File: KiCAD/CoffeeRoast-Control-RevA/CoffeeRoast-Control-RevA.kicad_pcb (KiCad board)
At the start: 2 copper layers, 100 x 75 mm, 26 parts, among them J1 24V_IN_FROM_230V_PSU_3A, J2 FAN_24V_PWM_3A, J3 SSR_INPUT_TO_EXTERNAL_SSR, J4 K_TYPE_THERMOCOUPLE, J5 USB_DATA_PANEL_HEADER, Q1 IRLZ44N_OR_LOGIC_NMOS, Q2 2N7002_SSR_DRIVER, SW1 RESET_EN, SW2 BOOT, U1 ESP32-S3-WROOM-1, U2 MAX6675_SOIC8_3V3, U3 AMS1117-3.3, U4 24V_TO_5V_BUCK_MODULE_>=1A

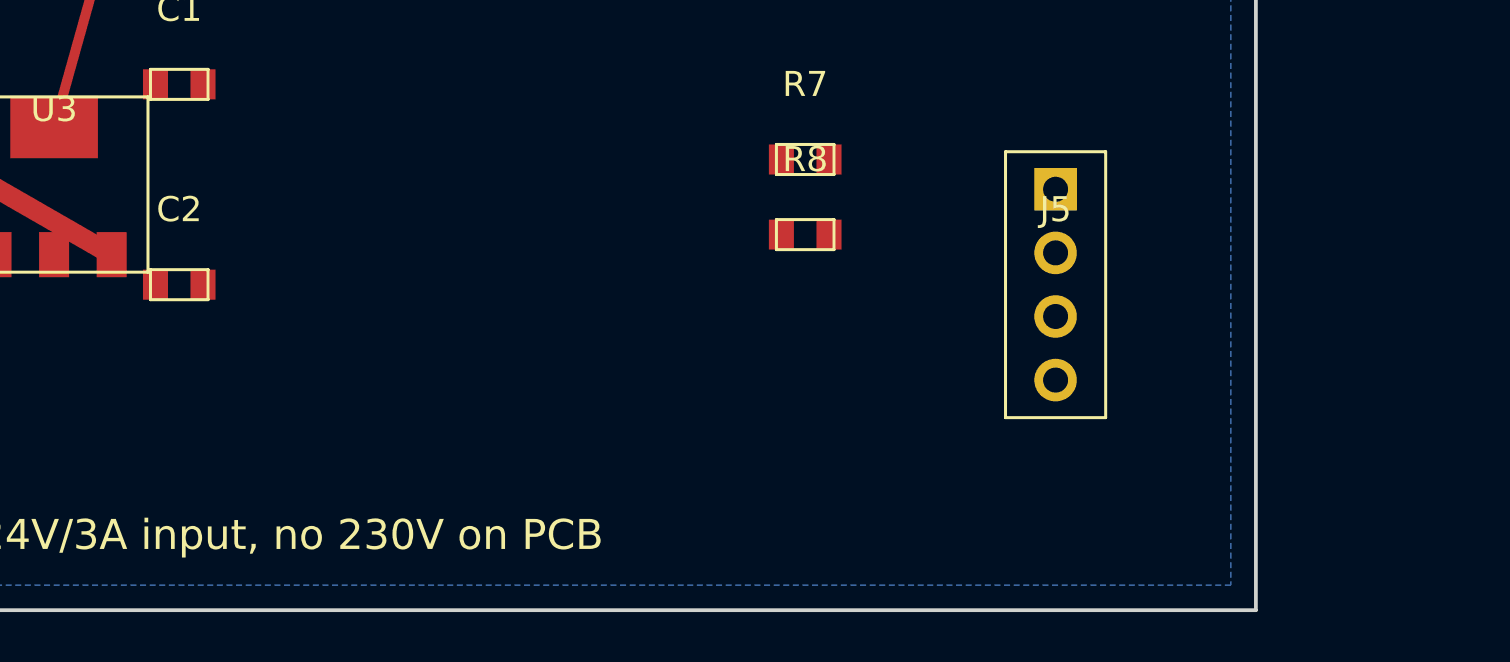
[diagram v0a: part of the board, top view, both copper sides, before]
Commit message: Put USB-C connector on CoffeeRoast control PCB
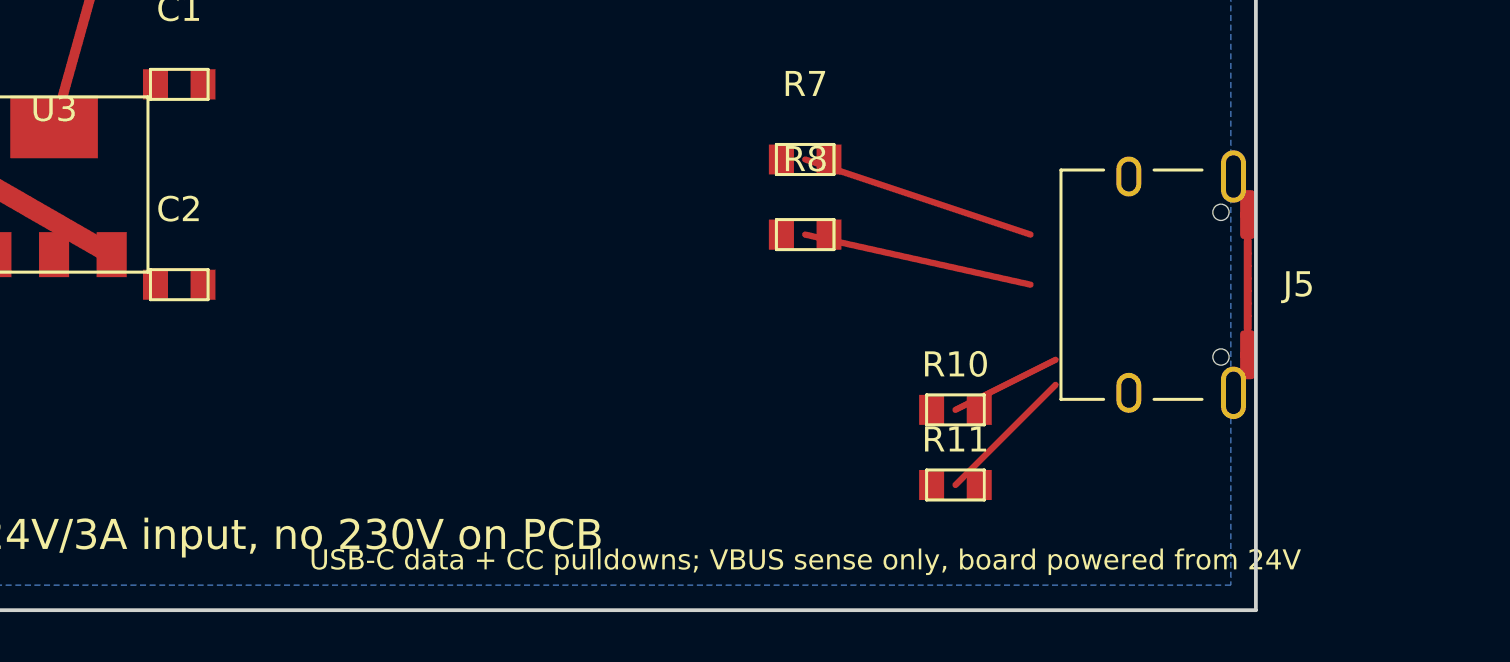
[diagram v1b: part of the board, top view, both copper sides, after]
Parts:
- added R10: 5k1_CC1_RD, CoffeeRoast:R_0805, F.Cu at (88.0, 67.0)
- added R11: 5k1_CC2_RD, CoffeeRoast:R_0805, F.Cu at (88.0, 70.0)
- J5: value USB_DATA_PANEL_HEADER -> USB_C_Receptacle_XKB_U262-16XN-4BVC11; footprint CoffeeRoast:PinHeader_1x4_P2.54mm -> Connector_USB:USB_C_Receptacle_XKB_U262-16XN-4BVC11
- moved J5 4.00 mm to (96.0, 62.0), turned to -90 degrees
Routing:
- net USB_DN: track 0.00 -> 9.49 mm
- net USB_DP: track 0.00 -> 9.22 mm
- net USB_CC2: track 0.00 -> 5.66 mm
- net USB_CC1: track 0.00 -> 4.47 mm
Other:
- board text added: "USB-C data + CC pulldowns; VBUS sense only, board powered from 24V"

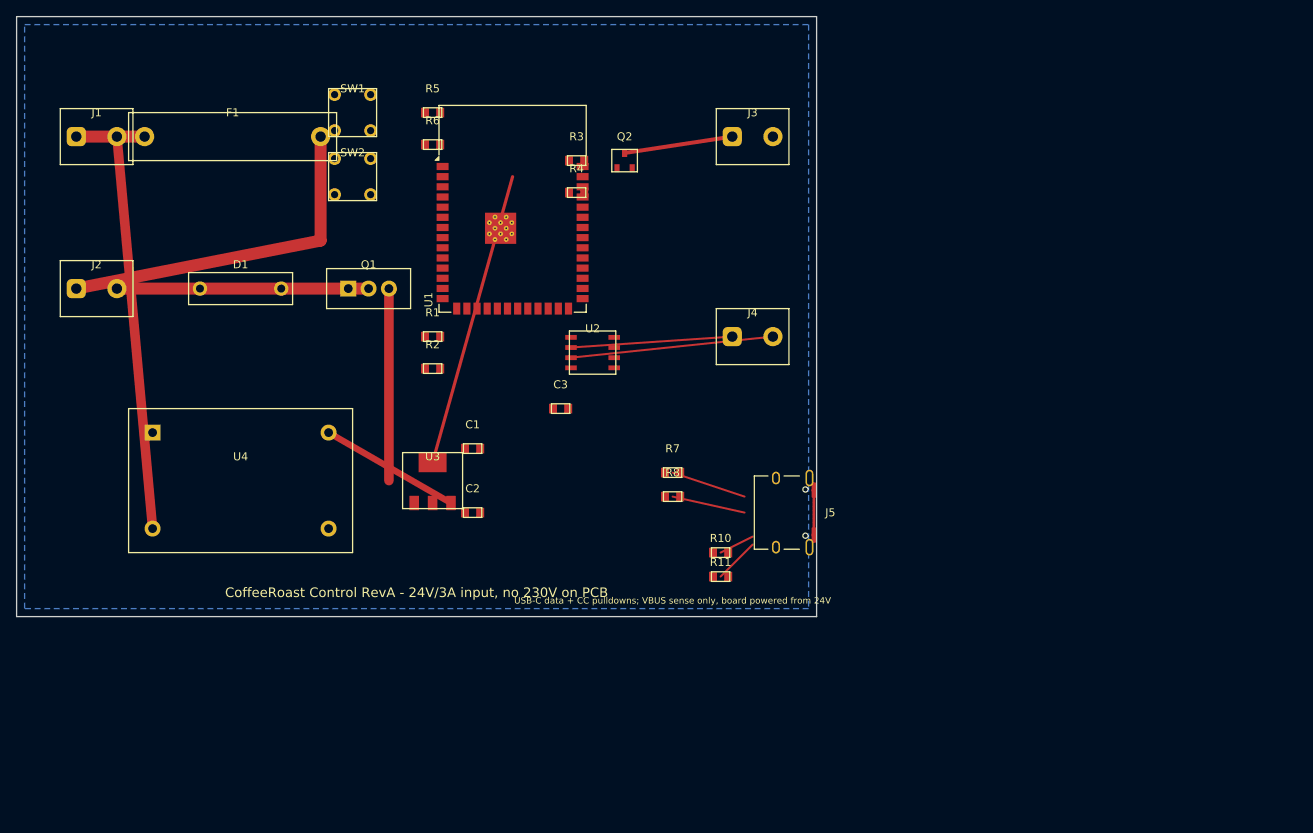
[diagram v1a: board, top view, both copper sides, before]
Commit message: Render CoffeeRoast PCB with KiCad
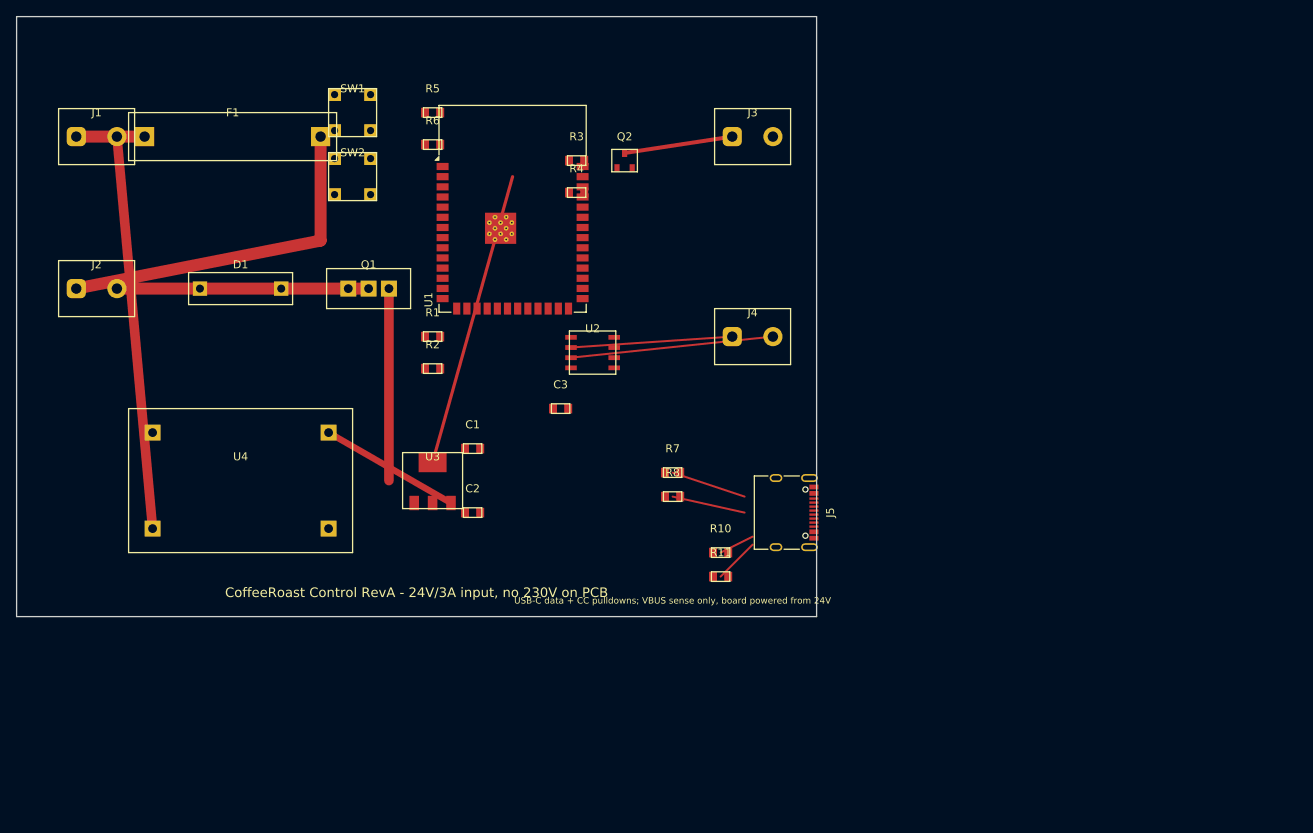
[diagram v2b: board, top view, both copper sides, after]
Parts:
- C1, C2, C3: footprint CoffeeRoast:C_0805 -> (none)
- D1: footprint CoffeeRoast:Diode_THT_P10.16mm -> (none)
- F1: footprint CoffeeRoast:Fuseholder_5x20mm_inline -> (none)
- J1, J2, J3, J4: footprint CoffeeRoast:TerminalBlock_2P_5.08mm -> (none)
- J5: footprint Connector_USB:USB_C_Receptacle_XKB_U262-16XN-4BVC11 -> USB_C_Receptacle_XKB_U262-16XN-4BVC11
- Q1: footprint CoffeeRoast:TO-220-3_Vertical -> (none)
- Q2: footprint CoffeeRoast:SOT-23 -> (none)
- R1, R10, R11, R2, R3, R4, R5, R6, R7, R8: footprint CoffeeRoast:R_0805 -> (none)
- SW1, SW2: footprint CoffeeRoast:SW_Tactile_6x6mm -> (none)
- U1: footprint RF_Module:ESP32-S3-WROOM-1 -> ESP32-S3-WROOM-1
- U2: footprint CoffeeRoast:SOIC-8_3.9x4.9mm_P1.27mm -> (none)
- U3: footprint CoffeeRoast:SOT-223-3_TabPin2 -> (none)
- U4: footprint CoffeeRoast:Buck_Module_24V_to_5V_4Pin -> (none)
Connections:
- U2 pad 8: (no net) -> GND
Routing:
- net GND: track 73.2 -> 83.3 mm
- net USB_CC2: track 5.66 -> 0.00 mm
- net USB_CC1: track 4.47 -> 0.00 mm
- removed copper zone on B.Cu, net GND

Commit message: Autoroute CoffeeRoast control PCB
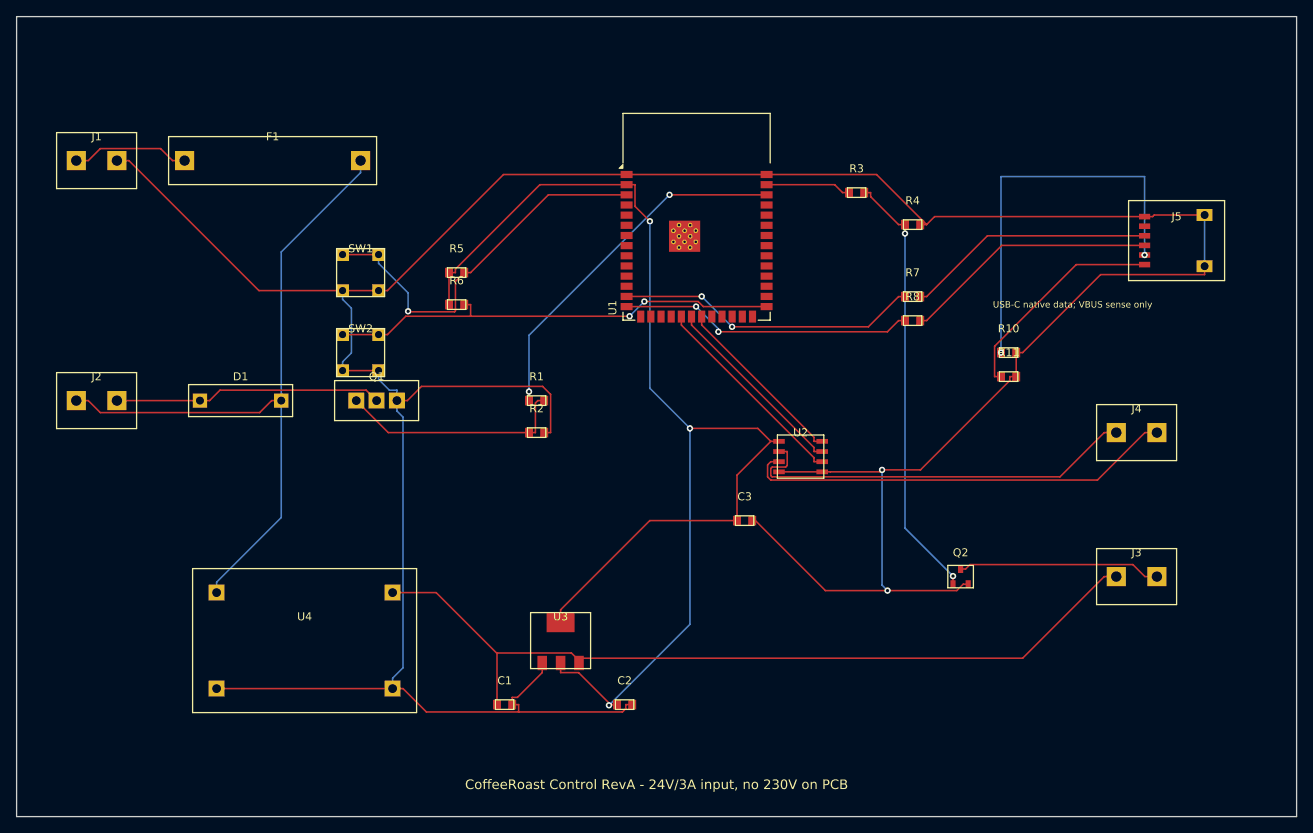
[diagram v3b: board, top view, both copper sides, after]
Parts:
- J5: value USB_C_Receptacle_XKB_U262-16XN-4BVC11 -> USB_C_RECEPTACLE_DRAFT_6PIN; footprint USB_C_Receptacle_XKB_U262-16XN-4BVC11 -> (none)
- moved J3 73.0 mm to (140.0, 70.0)
- moved Q2 66.8 mm to (118.0, 70.0)
- moved J5 59.6 mm to (145.0, 28.0), turned to 0 degrees
- moved J4 49.5 mm to (140.0, 52.0)
- moved R10 43.8 mm to (124.0, 42.0)
- moved R11 43.8 mm to (124.0, 45.0)
- moved R4 42.2 mm to (112.0, 26.0)
- moved R7 37.2 mm to (112.0, 35.0)
- moved R8 37.2 mm to (112.0, 38.0)
- moved R3 35.2 mm to (105.0, 22.0)
- moved C1 32.2 mm to (61.0, 86.0)
- moved C2 30.6 mm to (76.0, 86.0)
- moved U2 29.1 mm to (98.0, 55.0)
- moved C3 26.9 mm to (91.0, 63.0)
- moved U3 25.6 mm to (68.0, 78.0)
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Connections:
- J5 pad S1: (no net) -> GND
- U1 pad 41: GND -> (no net)
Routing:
- net GND: track 83.3 -> 418.0 mm, vias 0 -> 2
- net +3V3: track 37.1 -> 166.0 mm, vias 0 -> 3
- net +5V: track 17.7 -> 105.2 mm
- net BOOT: track 0.00 -> 57.2 mm, vias 0 -> 2
- net SSR_GATE: track 0.00 -> 54.5 mm, vias 0 -> 2
- net USB_CC1: track 0.00 -> 49.8 mm, vias 0 -> 2
- net EN: track 0.00 -> 48.7 mm, vias 0 -> 1
- net FAN_PWM: track 0.00 -> 45.1 mm, vias 0 -> 2
- net +24V_FUSED: track 44.1 -> 88.3 mm
- net USB_DN_MCU: track 0.00 -> 37.9 mm, vias 0 -> 2
- net USB_DP_MCU: track 0.00 -> 36.9 mm, vias 0 -> 2
- net THERMO_PLUS: track 20.2 -> 51.4 mm
- net THERMO_MINUS: track 25.4 -> 54.4 mm
- net FAN_GATE: track 0.00 -> 29.0 mm
- net USB_CC2: track 0.00 -> 27.6 mm
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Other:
- board size 100 x 75 mm -> 160 x 100 mm
- board text added: "ESP32 ANTENNA KEEPOUT - no copper"
- board text added: "USB-C native data; VBUS sense only"
- board text removed: "ESP32 ANTENNA KEEPOUT - no copper / keep at board edge"
- board text removed: "USB-C data + CC pulldowns; VBUS sense only, board powered from 24V"

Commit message: Replace USB-C draft with exact connector footprint
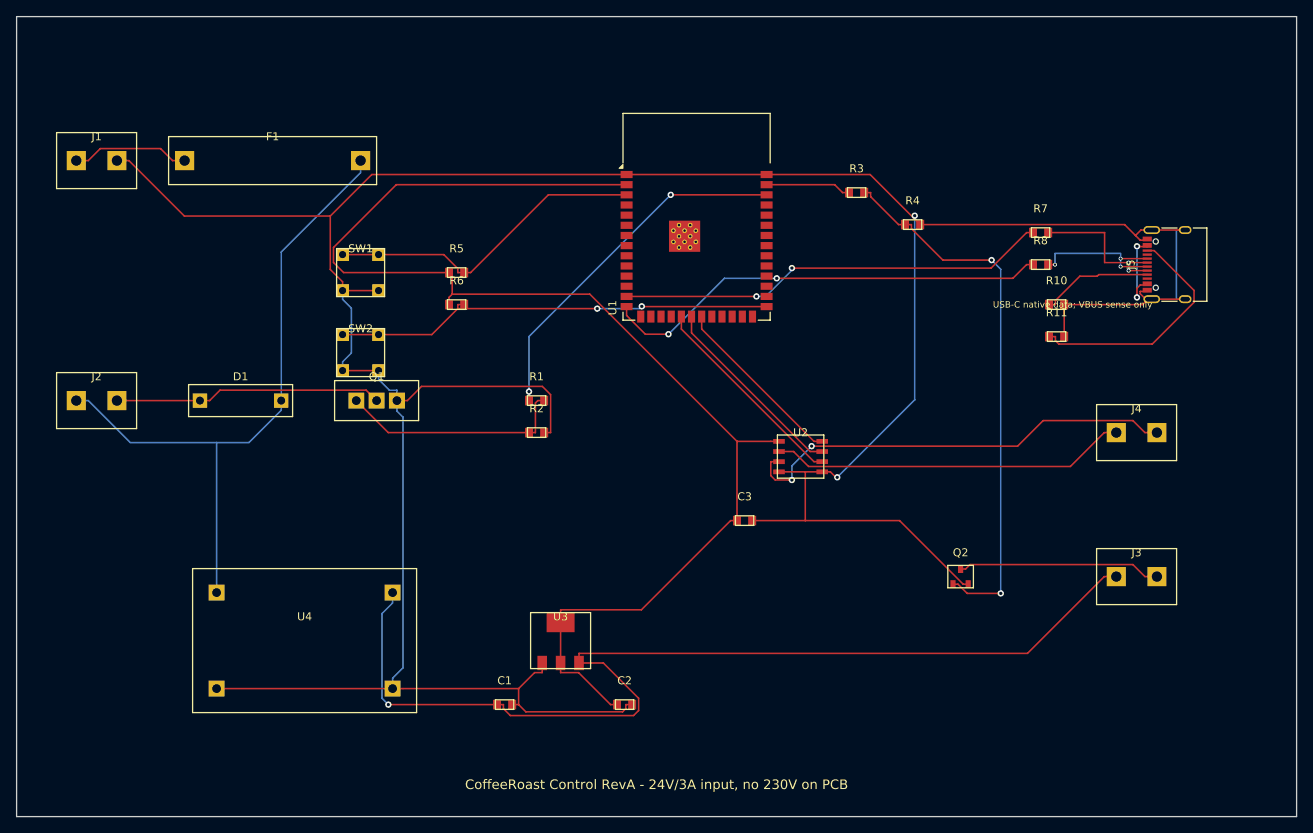
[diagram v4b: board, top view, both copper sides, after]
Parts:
- J5: value USB_C_RECEPTACLE_DRAFT_6PIN -> USB_C_Receptacle_XKB_U262-16XN-4BVC11; footprint (none) -> USB_C_Receptacle_XKB_U262-16XN-4BVC11
- moved R7 17.9 mm to (128.0, 27.0)
- moved R8 17.5 mm to (128.0, 31.0)
- moved R10 8.49 mm to (130.0, 36.0)
- moved R11 7.81 mm to (130.0, 40.0)
- moved J5 3.00 mm to (145.0, 31.0), turned to 90 degrees
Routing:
- net USB_CC1: track 49.8 -> 14.1 mm, vias 2 -> 0
- net +5V: track 105.2 -> 130.4 mm, vias 0 -> 1
- net USB_DP_MCU: track 36.9 -> 56.5 mm
- net USB_DN_MCU: track 37.9 -> 54.3 mm
- net SSR_GATE: track 54.5 -> 68.6 mm
- net USB_DP: track 31.9 -> 18.8 mm, vias 0 -> 3
- net USB_DN: track 31.2 -> 19.5 mm, vias 0 -> 2
- net USB_VBUS: track 0.00 -> 10.9 mm, vias 0 -> 2
- net EN: track 48.7 -> 40.8 mm, vias 1 -> 0
- net THERMO_PLUS: track 51.4 -> 44.7 mm
- net +24V_FUSED: track 88.3 -> 83.5 mm
- net +3V3: track 166.0 -> 162.9 mm, vias 3 -> 0
- net USB_CC2: track 27.6 -> 30.4 mm
- net THERMO_MINUS: track 54.4 -> 56.0 mm, vias 0 -> 2
- net BOOT: track 57.2 -> 55.8 mm
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
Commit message: Expose ESP32 pins as debug pads
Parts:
- added TPESP1: GND, , F.Cu at (75.3, 19.7)
- added TPESP10: IO17, , F.Cu at (75.3, 31.2)
- added TPESP11: IO18, , F.Cu at (75.3, 32.4)
- added TPESP12: IO8, , F.Cu at (75.3, 33.7)
- added TPESP13: USB_D-/IO19, , F.Cu at (75.3, 35.0)
- added TPESP14: USB_D+/IO20, , F.Cu at (75.3, 36.2)
- added TPESP15: IO3, , F.Cu at (78.0, 38.3)
- added TPESP16: IO46, , F.Cu at (79.3, 38.5)
- added TPESP17: IO9, , F.Cu at (80.6, 38.5)
- added TPESP18: IO10, , F.Cu at (81.8, 38.5)
- added TPESP19: IO11/MAXDO, , F.Cu at (83.1, 38.5)
- added TPESP2: 3V3, , F.Cu at (75.3, 21.0)
- added TPESP20: IO12/MAXCS, , F.Cu at (84.4, 38.5)
- added TPESP21: IO13/MAXCLK, , F.Cu at (85.6, 38.5)
- added TPESP22: IO14, , F.Cu at (86.9, 38.5)
- added TPESP23: IO21, , F.Cu at (88.2, 38.5)
- added TPESP24: IO47, , F.Cu at (89.4, 38.5)
- added TPESP25: IO48, , F.Cu at (90.7, 38.5)
- added TPESP26: IO45, , F.Cu at (92.0, 38.5)
- added TPESP27: IO0/BOOT, , F.Cu at (94.7, 36.2)
- added TPESP28: IO35, , F.Cu at (94.7, 35.0)
- added TPESP29: IO36, , F.Cu at (94.7, 33.7)
- added TPESP3: EN, , F.Cu at (75.3, 22.3)
- added TPESP30: IO37, , F.Cu at (94.2, 32.4)
- added TPESP31: IO38, , F.Cu at (94.7, 31.2)
- added TPESP32: IO39, , F.Cu at (94.7, 29.9)
- added TPESP33: IO40, , F.Cu at (94.7, 28.6)
- added TPESP34: IO41, , F.Cu at (94.7, 27.4)
- added TPESP35: IO42, , F.Cu at (94.7, 26.1)
- added TPESP36: RXD0/IO44, , F.Cu at (94.7, 24.8)
- added TPESP37: TXD0/IO43, , F.Cu at (94.7, 23.6)
- added TPESP38: IO2/FAN, , F.Cu at (94.7, 22.3)
- added TPESP39: IO1/SSR, , F.Cu at (94.7, 21.0)
- added TPESP4: IO4, , F.Cu at (75.3, 23.6)
- added TPESP40: GND, , F.Cu at (94.7, 19.7)
- added TPESP5: IO5, , F.Cu at (75.3, 24.8)
- added TPESP6: IO6, , F.Cu at (75.3, 26.1)
- added TPESP7: IO7, , F.Cu at (75.3, 27.4)
- added TPESP8: IO15, , F.Cu at (75.3, 28.6)
- added TPESP9: IO16, , F.Cu at (75.3, 29.9)
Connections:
- U1 pad 10: (no net) -> GPIO17
- U1 pad 11: (no net) -> GPIO18
- U1 pad 12: (no net) -> GPIO8
- U1 pad 15: (no net) -> GPIO3
- U1 pad 16: (no net) -> GPIO46
- U1 pad 17: (no net) -> GPIO9
- U1 pad 18: (no net) -> GPIO10
- U1 pad 22: (no net) -> GPIO14
- U1 pad 23: (no net) -> GPIO21
- U1 pad 24: (no net) -> GPIO47
- U1 pad 25: (no net) -> GPIO48
- U1 pad 26: (no net) -> GPIO45
- U1 pad 28: (no net) -> GPIO35
- U1 pad 29: (no net) -> GPIO36
- U1 pad 30: (no net) -> GPIO37
- U1 pad 31: (no net) -> GPIO38
- U1 pad 32: (no net) -> GPIO39
- U1 pad 33: (no net) -> GPIO40
- U1 pad 34: (no net) -> GPIO41
- U1 pad 35: (no net) -> GPIO42
- U1 pad 36: (no net) -> RXD0_GPIO44
- U1 pad 37: (no net) -> TXD0_GPIO43
- U1 pad 4: (no net) -> GPIO4
- U1 pad 5: (no net) -> GPIO5
- U1 pad 6: (no net) -> GPIO6
- U1 pad 7: (no net) -> GPIO7
- U1 pad 8: (no net) -> GPIO15
- U1 pad 9: (no net) -> GPIO16
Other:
- board text added: "TPESP1-40 ESP32 debug pads (map in docs)"
- board text added: "TPESP10:IO17"
- board text added: "TPESP11:IO18"
- board text added: "TPESP12:IO8"
- board text added: "TPESP13:USB_D-/IO19"
- board text added: "TPESP14:USB_D+/IO20"
- board text added: "TPESP15:IO3"
- board text added: "TPESP16:IO46"
- board text added: "TPESP17:IO9"
- board text added: "TPESP18:IO10"
- board text added: "TPESP19:IO11/MAXDO"
- board text added: "TPESP1:GND"
- board text added: "TPESP20:IO12/MAXCS"
- board text added: "TPESP21:IO13/MAXCLK"
- board text added: "TPESP22:IO14"
- board text added: "TPESP23:IO21"
- board text added: "TPESP24:IO47"
- board text added: "TPESP25:IO48"
- board text added: "TPESP26:IO45"
- board text added: "TPESP27:IO0/BOOT"
- board text added: "TPESP28:IO35"
- board text added: "TPESP29:IO36"
- board text added: "TPESP2:3V3"
- board text added: "TPESP30:IO37"
- board text added: "TPESP31:IO38"
- board text added: "TPESP32:IO39"
- board text added: "TPESP33:IO40"
- board text added: "TPESP34:IO41"
- board text added: "TPESP35:IO42"
- board text added: "TPESP36:RXD0/IO44"
- board text added: "TPESP37:TXD0/IO43"
- board text added: "TPESP38:IO2/FAN"
- board text added: "TPESP39:IO1/SSR"
- board text added: "TPESP3:EN"
- board text added: "TPESP40:GND"
- board text added: "TPESP4:IO4"
- board text added: "TPESP5:IO5"
- board text added: "TPESP6:IO6"
- board text added: "TPESP7:IO7"
- board text added: "TPESP8:IO15"
- board text added: "TPESP9:IO16"
